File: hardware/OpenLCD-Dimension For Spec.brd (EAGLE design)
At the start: 45.7 x 24.1 mm, 29 parts, among them J1 JST, J2 PTH, J3 3.5mm Screw Terminal, J4 Reset, Q1 PNP-500mA, U1 ATMEGA328P_TQFP, U2 4BIT-LCD, U4 MCP4725, Y2 16MHZ

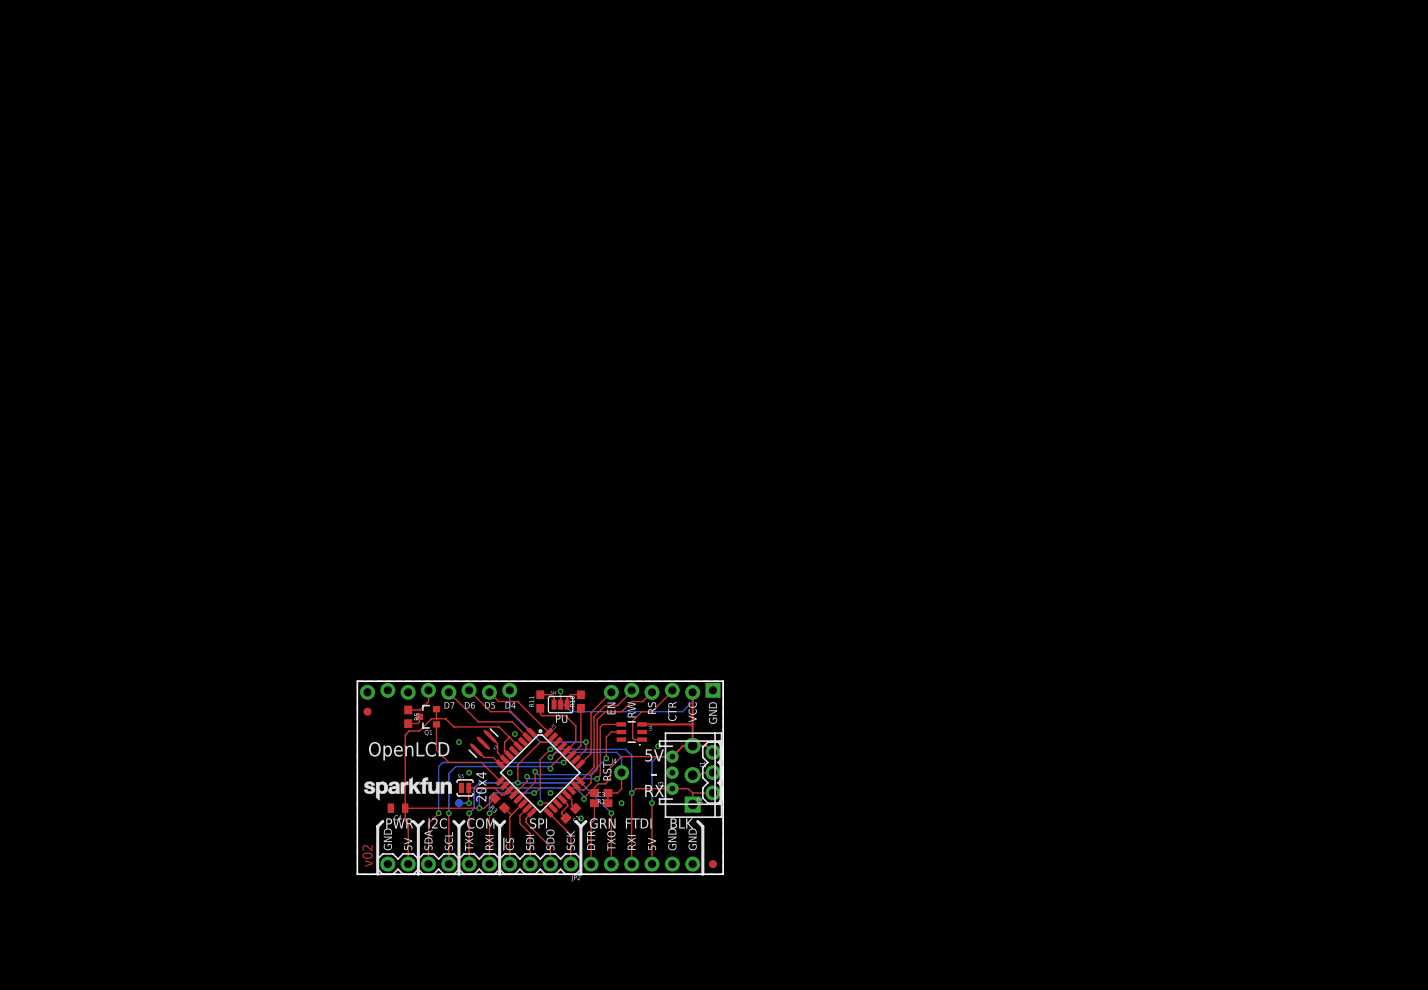
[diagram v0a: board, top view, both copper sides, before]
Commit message: Changes the pins to work with v2 protos. Added custom char support.
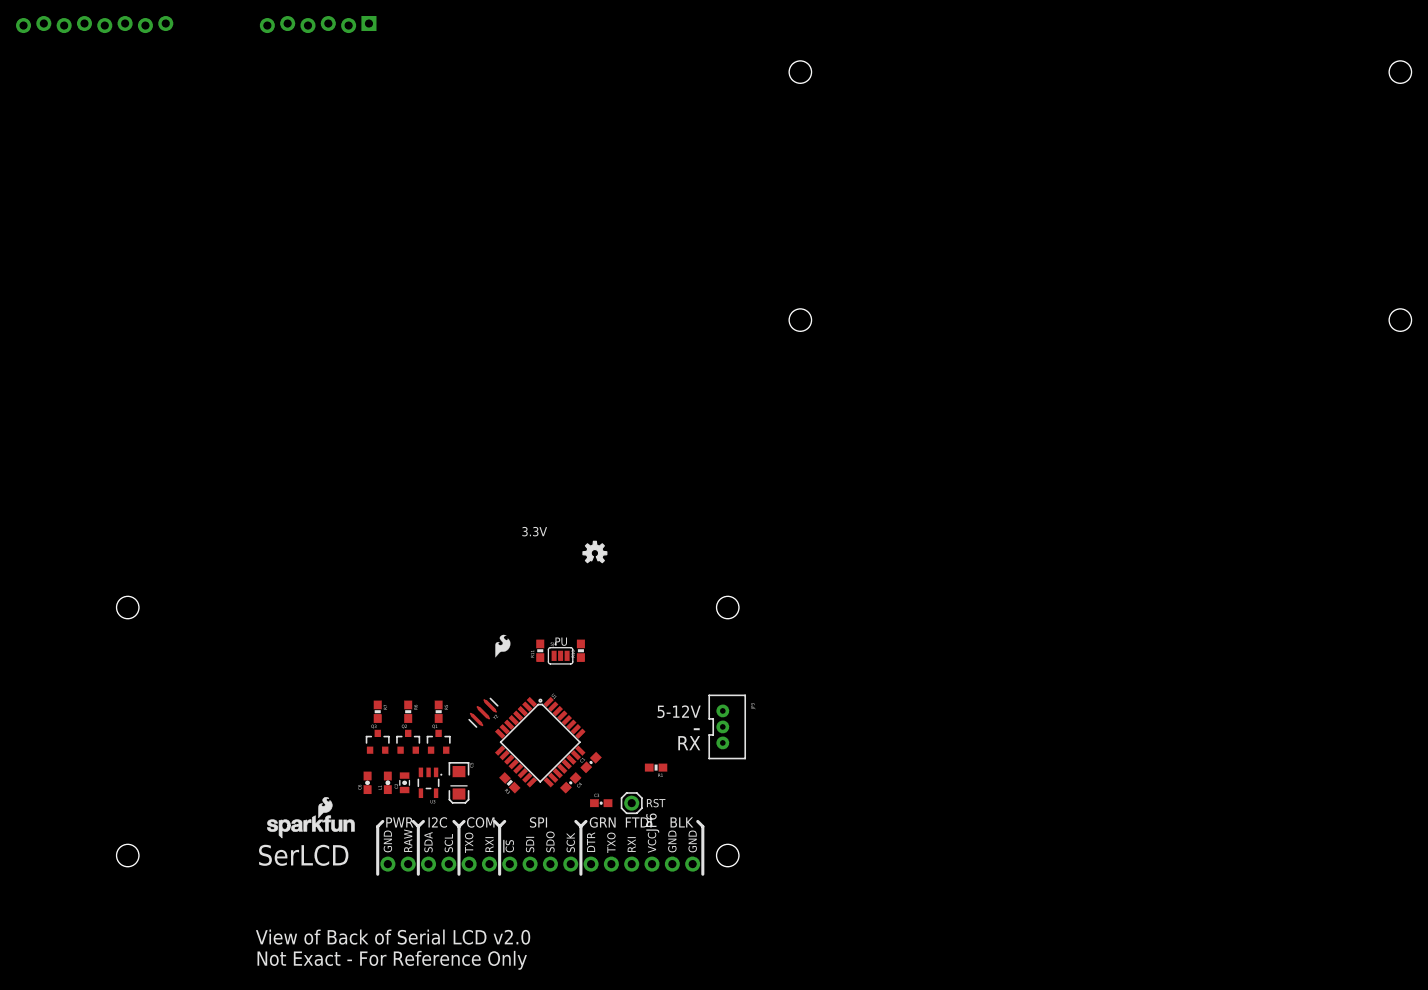
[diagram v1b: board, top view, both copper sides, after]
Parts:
- removed FID1, FID2: FIDUCIAL1X2, SparkFun-Aesthetics:FIDUCIAL-1X2
- removed J1: JST, SparkFun-Connectors:JST-3-PTH
- removed J2: PTH, SparkFun-Connectors:1X03
- removed J3: 3.5mm Screw Terminal, SparkFun-Connectors:SCREWTERMINAL-3.5MM-3_LOCK.007S
- removed J4: Reset, SparkFun-Connectors:1X01_NO_SILK
- removed LOGO3: SFE_LOGO_NAME.1_INCH, SparkFun-Aesthetics:SFE_LOGO_NAME_.1
- removed LOGO4: SFE_LOGO_FLAME.1_STOP, SparkFun-Aesthetics:SFE_LOGO_FLAME_STOP_.1
- removed SJ5: Size, SparkFun-Passives:PAD-JUMPER-2-NO_YES_SILK
- removed TP2: (no value), SparkFun-Passives:PAD.03X.04
- removed U4: MCP4725, SparkFun-AnalogIC:SOT23-6
- added C2: 1.0uF/25V, SparkFun-Capacitors:0805-CAP
- added C5: 10uF, SparkFun-Capacitors:EIA3216
- added C6: (no value), SparkFun-Passives:0603-CAP
- added JP3: 3-PIN SMD, SparkFun-Connectors:JST-3-PTH-VERT
- added JP6: RESET, SparkFun-Connectors:1X01
- added L1: (no value), SparkFun-Passives:0603
- added LOGO1: SFE_LOGO_NAME_FLAME.1_INCH, SparkFun-Aesthetics:SFE_LOGO_NAME_FLAME_.1
- added Q2, Q3: PNP-500mA, SparkFun-DiscreteSemi:SOT23-3
- added R6, R7: 240, SparkFun-Resistors:0603-RES
- added U3: MIC5205-ADJ, SparkFun-PowerIC:SOT23-5
- C1, C3: device SparkFun-Capacitors:0603 -> SparkFun-Capacitors:0603-CAP
- C4: value 10uF -> 0.1uF; device SparkFun-Capacitors:0805 -> SparkFun-Capacitors:0603-CAP
- R1, R3: value 10k -> 10K; device SparkFun-Resistors:0603 -> SparkFun-Resistors:0603-RES
- R10, R11: value 4.7k -> 4.7K; device SparkFun-Resistors:0603 -> SparkFun-Resistors:0603-RES
- R5: device SparkFun-Resistors:0603 -> SparkFun-Resistors:0603-RES
- U2: value 4BIT-LCD -> 4BIT-RGB
- Y2: value 16MHZ -> 11.0592MHZ
- moved U2 93.8 mm to (-30.6, 90.7)
- moved FRAME1 41.9 mm to (-49.0, -28.0)
- moved U$4 36.8 mm to (29.7, 40.1), flipped to the top
- moved C4 21.8 mm to (26.7, 11.4), turned to 225 degrees
- moved U$1 17.1 mm to (17.3, 27.1), flipped to the top
- moved R1 7.56 mm to (37.3, 13.3)
- moved C1 6.84 mm to (29.2, 14.0), turned to 45 degrees
- moved R10 6.35 mm to (27.9, 27.9)
- moved R11 6.35 mm to (22.9, 27.9)
- moved SJ4 6.10 mm to (25.4, 27.3)
- moved R5 3.86 mm to (10.2, 20.3)
- moved U1 3.81 mm to (22.9, 16.5)
- moved Y2 3.81 mm to (15.7, 20.2)
- moved Q1 3.42 mm to (10.2, 16.5), turned to 0 degrees
- moved R3 2.84 mm to (19.1, 11.4)
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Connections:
- net BL-CONTROL renamed BL-R/W
- removed net BACKLIGHT: R5.1, U2.15
- removed net BLU: U2.18
- removed net CONTRAST: U2.3, U4.1
- removed net GRN: U2.17
- removed net SW-SCL: U1.13, U4.5
- removed net SW-SDA: U1.12, U4.4
- new net A-BLUE: R7.1, U2.18
- new net A-GREEN: R6.1, U2.17
- new net BACKLIGHT1: U2.15
- new net BACKLIGHT2: U2.16
- new net BL-B: Q3.1, U1.11
- new net BL-G: Q2.1, U1.10
- new net CONTRAST-PWM: L1.1, U1.13
- new net MONO/RED: R5.1
- new net N$4: Q2.3, R6.2
- new net N$5: Q3.3, R7.2
- new net RAW: C2.1, JP2.9, JP3.1, U3.1, U3.3
- new net VO-CONTRAST: C6.1, L1.2, U2.3
- net GND: now also C2.2, C4.1, C5.C, C6.2, JP3.2, U3.2; no longer C4.2, J1.2, J2.2, J3.2, SJ5.1, U2.16, U4.2, U4.6
- net RST: now also JP6.1; no longer J4.1
- net RXI: now also JP3.3; no longer J1.3, J2.1, J3.1
- net SIZE: now also U1.12; no longer SJ5.2, TP2.P$1, U1.11
- net VCC: now also C4.2, C5.A, Q2.2, Q3.2, U3.5; no longer C4.1, J1.1, J2.3, J3.3, JP2.9, U4.3
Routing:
- net VCC: track 138.9 -> 0.00 mm, vias 5 -> 0
- net RXI: track 58.0 -> 0.00 mm, vias 4 -> 0
- net TXO: track 43.2 -> 0.00 mm, vias 3 -> 0
- net SCL: track 36.9 -> 0.00 mm, vias 2 -> 0
- net SDA: track 36.2 -> 0.00 mm, vias 2 -> 0
- net SW-SDA: track 21.4 -> 0.00 mm, vias 2 -> 0
- net SW-SCL: track 19.4 -> 0.00 mm, vias 2 -> 0
- net RS: track 19.0 -> 0.00 mm
- net RST: track 18.6 -> 0.00 mm, vias 1 -> 0
- net D4: track 16.5 -> 0.00 mm, vias 1 -> 0
- net R/W: track 14.9 -> 0.00 mm
- net BL-R/W: track 12.8 -> 0.00 mm
- net D7: track 12.1 -> 0.00 mm
- net EN: track 10.6 -> 0.00 mm
- net D6: track 10.0 -> 0.00 mm
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- removed copper zone on layer 1, net GND
- removed copper zone on layer 16, net GND
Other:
- board outline removed
- board text added: "3.3V"
- board text added: "5-12V"
- board text added: "RAW"
- board text added: "SerLCD"
- board text added: "View of Back of Serial LCD v2.0 Not Exact - For Reference Only"
- board text removed: "20x4"
- board text removed: "5V"
- board text removed: "CTR"
- board text removed: "D4"
- board text removed: "D5"
- board text removed: "D6"
- board text removed: "D7"
- board text removed: "EN"
- board text removed: "N. Seidle"
- board text removed: "OpenLCD"
- board text removed: "RS"
- board text removed: "RW"
- board text removed: "This side towards LCD"
- board text removed: "v02"
